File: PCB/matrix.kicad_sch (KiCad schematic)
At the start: 27 parts, among them SW10 EC_SW, SW11 EC_SW, SW12 EC_SW, SW13 EC_SW, SW14 EC_SW, SW15 EC_SW, SW16 EC_SW, SW17 EC_SW, SW18 EC_SW, SW19 EC_SW, SW2 EC_SW, SW20 EC_SW, SW21 EC_SW, SW22 EC_SW, SW23 EC_SW, SW24 EC_SW, SW25 EC_SW, SW26 EC_SW, SW27 EC_SW, SW28 EC_SW, SW3 EC_SW, SW4 EC_SW, SW5 EC_SW, SW6 EC_SW, SW7 EC_SW, SW8 EC_SW, SW9 EC_SW

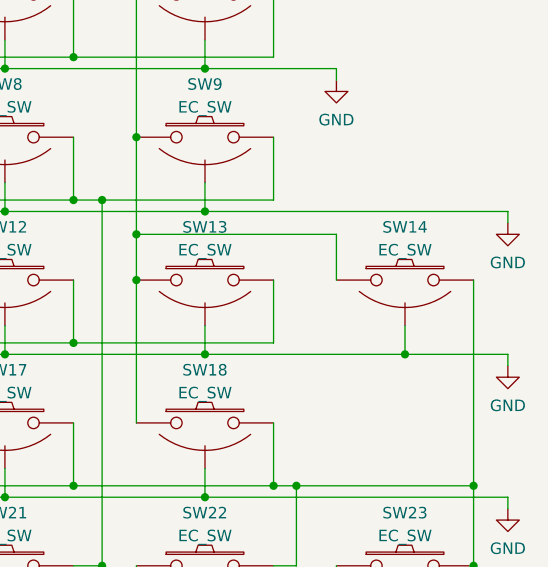
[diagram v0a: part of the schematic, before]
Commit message: Update for 3d models
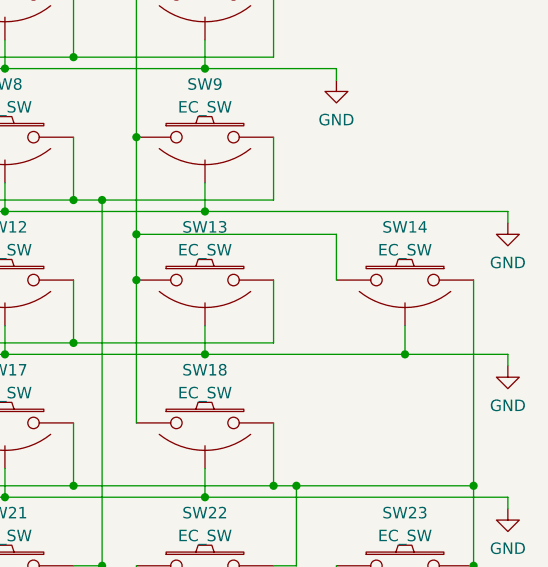
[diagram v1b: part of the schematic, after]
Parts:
- SW10, SW11, SW12, SW13, SW15, SW16, SW17, SW18, SW19, SW2, SW20, SW21, SW22, SW24, SW25, SW26, SW27, SW3, SW4, SW5, SW6, SW7, SW8, SW9: footprint cipulot_parts:ecs_pad_no_ring -> cipulot_parts:ecs_pad_1U_no_ring
- SW14, SW23, SW28: footprint cipulot_parts:ecs_pad_no_ring -> cipulot_parts:ecs_pad_2U_no_ring
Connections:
- net SENSE_3: now also SW14.2; no longer SW14.1
- net STROBE_3: now also SW14.1; no longer SW14.2
